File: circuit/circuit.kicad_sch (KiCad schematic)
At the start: 9 parts, among them J1 Input Audio Jack, U1 TLE2062

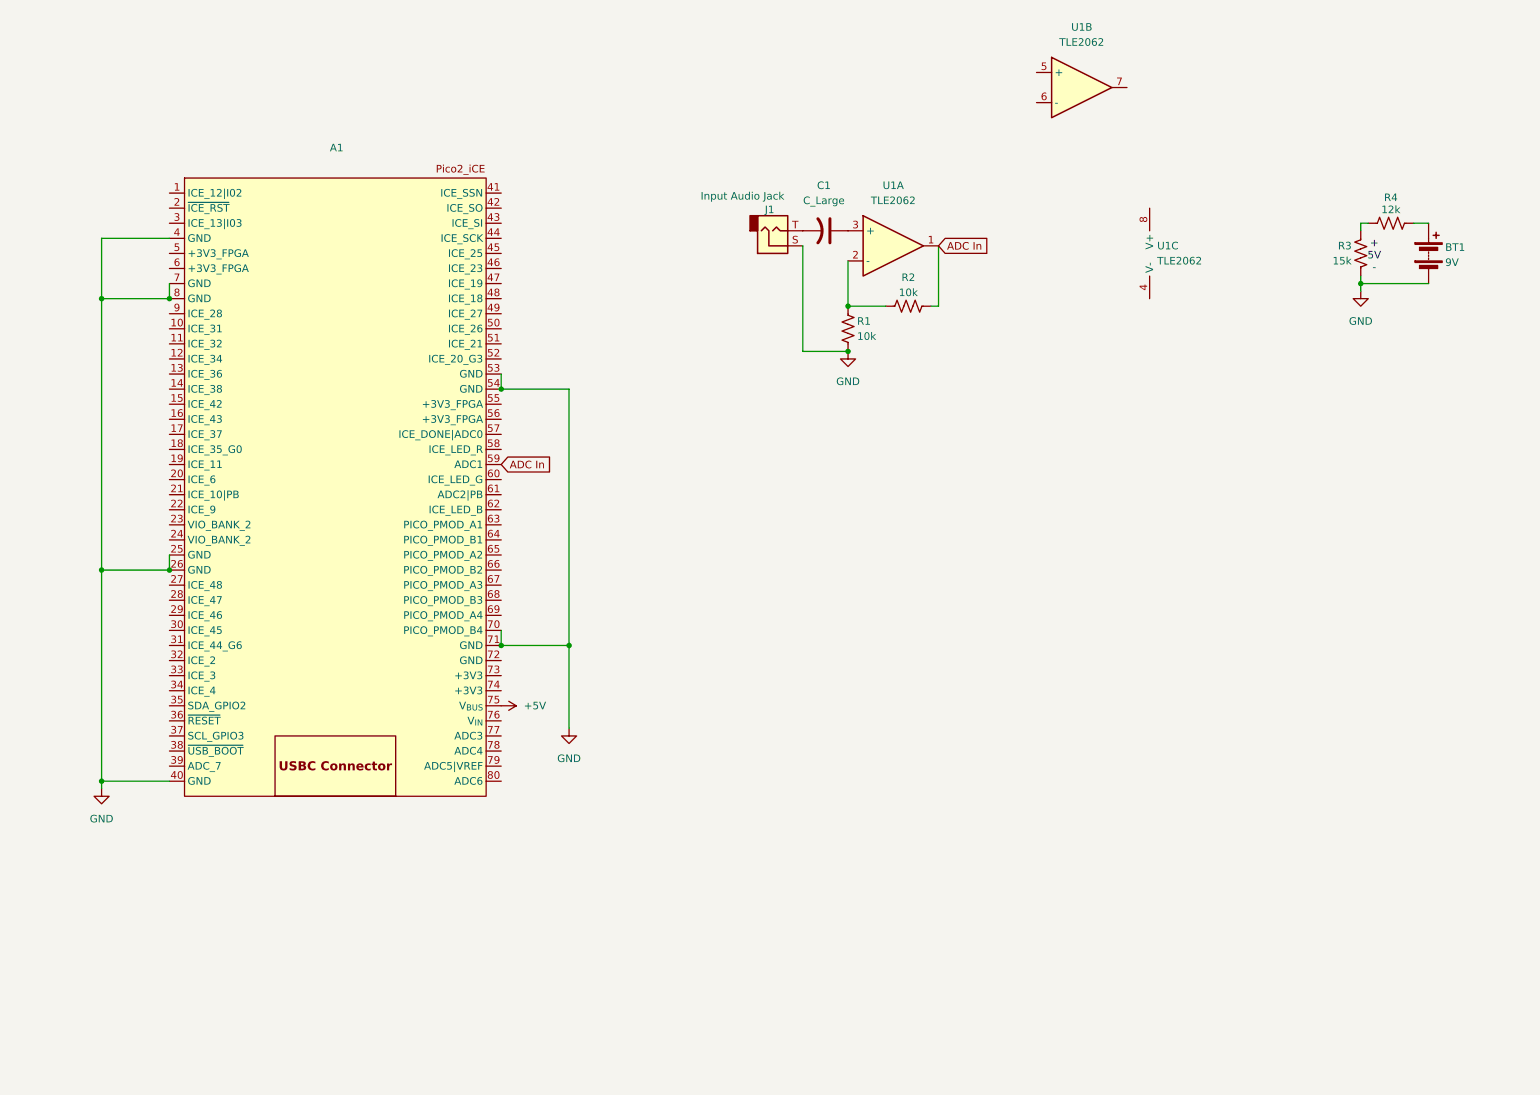
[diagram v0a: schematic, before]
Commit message: correct op amp added to schematic
in kicad
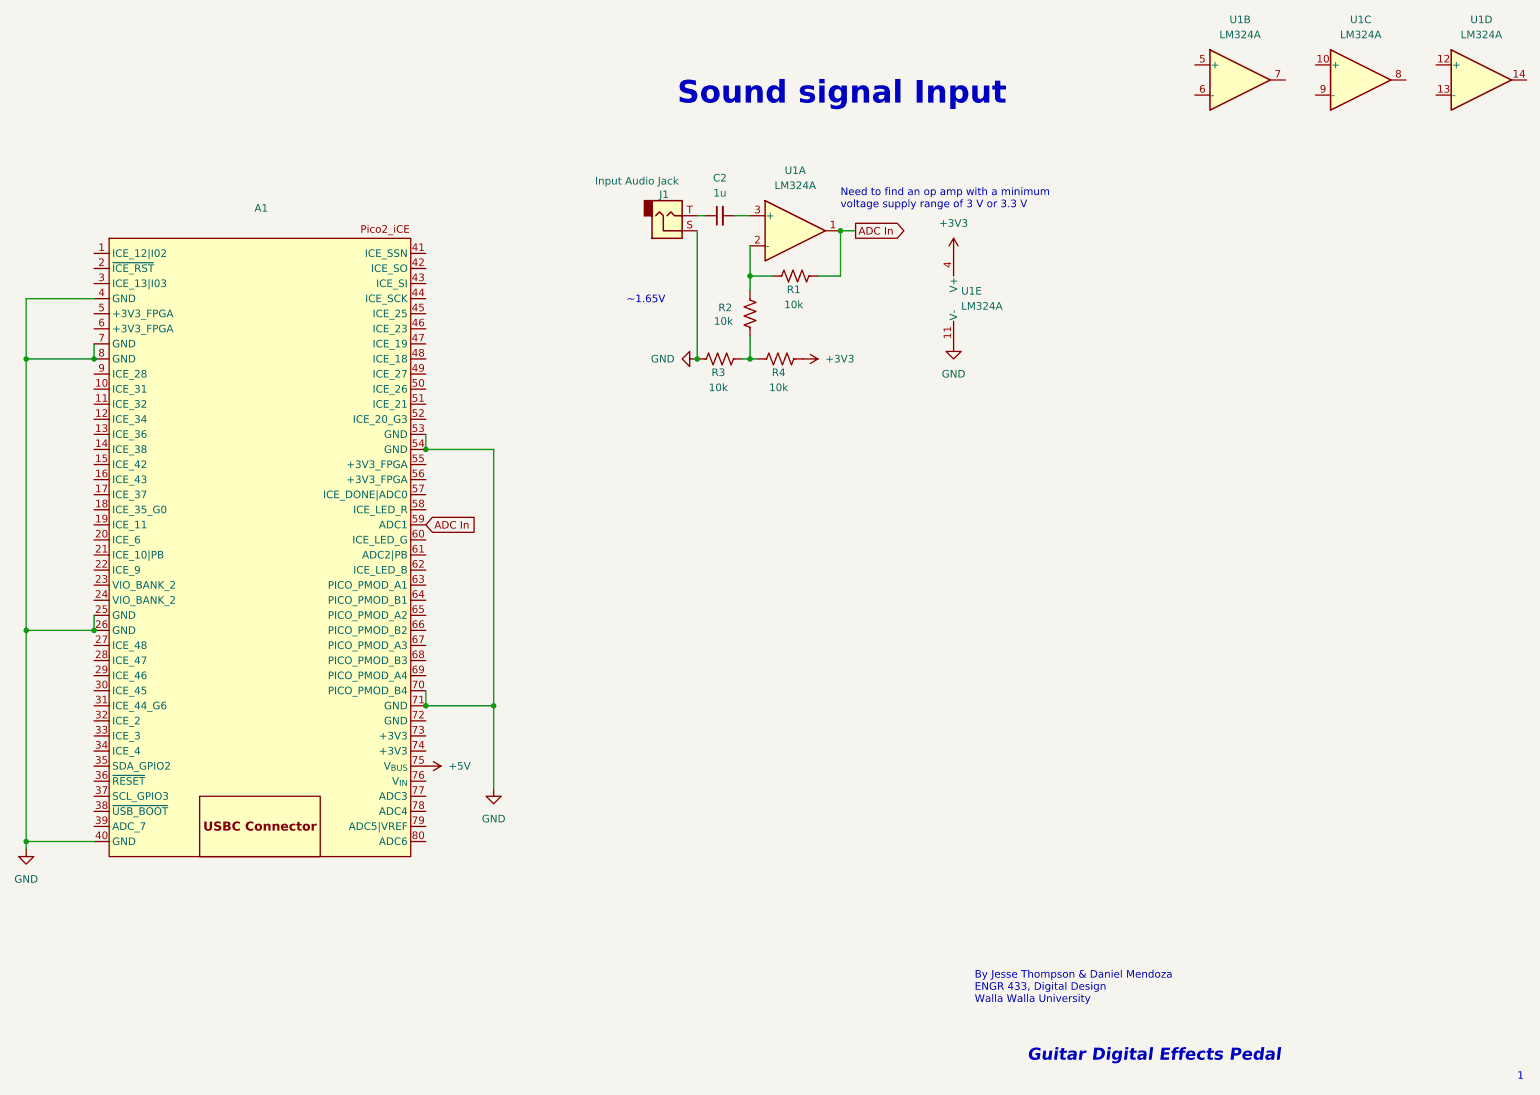
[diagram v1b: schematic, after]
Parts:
- removed BT1: 9V, symbol Device:Battery
- removed C1: C_Large, symbol Device:C_US
- removed U1: TLE2062, symbol Device:Opamp_Dual
- added C2: 1u, symbol Device:C_Small
- added U1: LM324A, symbol Amplifier_Operational:LM324A
- R3: value 15k -> 10k
- R4: value 12k -> 10k
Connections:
- net ADC In: now also R1.1, U1.1; no longer R2.2
- net GND: now also U1.11 (V-); no longer R1.2
- net at R2.1: now also R3.1, R4.2; no longer R1.1
- net at J1.T: now also C2.1
- net +3V3: now reaches R4.1
- net +3V3: now also U1.4 (V+); no longer R3.1
- new net: R1.2, R2.2, U1.2 (-)
- new net: C2.2, U1.3 (+)
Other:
- note added: "1"
- note added: "By Jesse Thompson & Daniel Mendoza ENGR 433, Digital Design Walla Walla University"
- note added: "Guitar Digital Effects Pedal"
- note added: "Need to find an op amp with a minimum voltage supply range of 3 V or 3.3 V"
- note added: "Sound signal Input"
- note added: "~1.65V"
- note removed: "+ 5V -"
- moved on the sheet: A1, J1

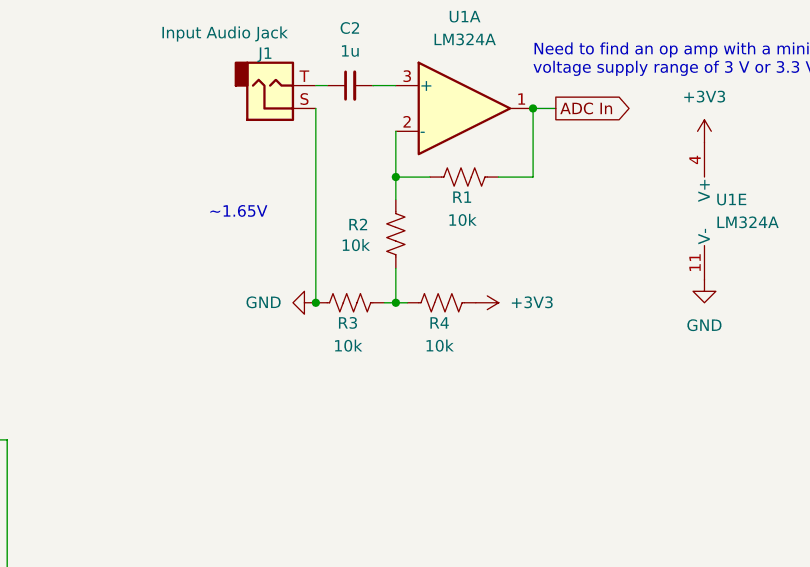
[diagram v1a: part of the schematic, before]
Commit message: First draft of verilog
Not tested but in theory "functional".
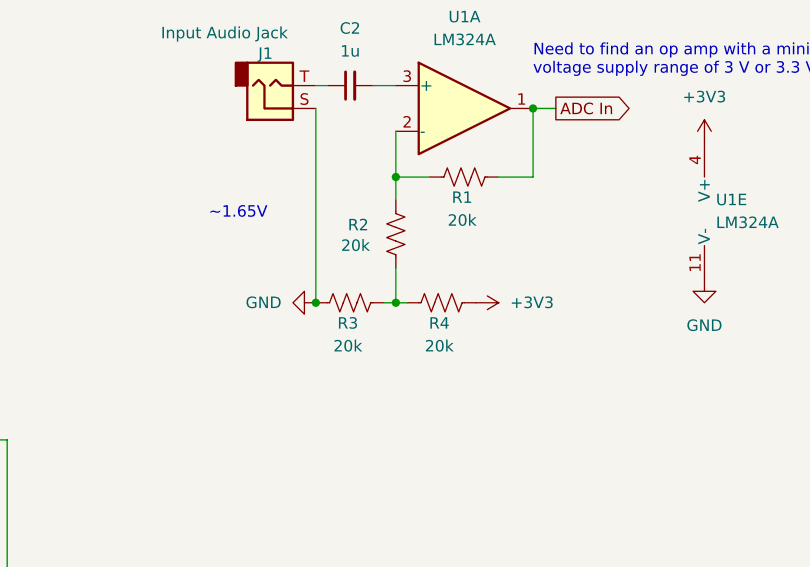
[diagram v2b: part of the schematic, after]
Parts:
- R1, R2, R3, R4: value 10k -> 20k
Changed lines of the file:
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@@
 			)
 		)
-		(property "Value" "10k"
+		(property "Value" "20k"
 			(at 144.526 77.216 90)
 			(effects
@@
 			)
 		)
-		(property "Value" "10k"
+		(property "Value" "20k"
 			(at 133.604 66.04 0)
 			(effects
@@
 			)
 		)
-		(property "Value" "10k"
+		(property "Value" "20k"
 			(at 134.366 77.216 90)
 			(effects
@@
 			)
 		)
-		(property "Value" "10k"
+		(property "Value" "20k"
 			(at 147.066 63.246 90)
 			(effects
